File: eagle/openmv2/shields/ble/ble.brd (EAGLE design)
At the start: 35.6 x 26.7 mm, 20 parts, among them U2 OPENMV3

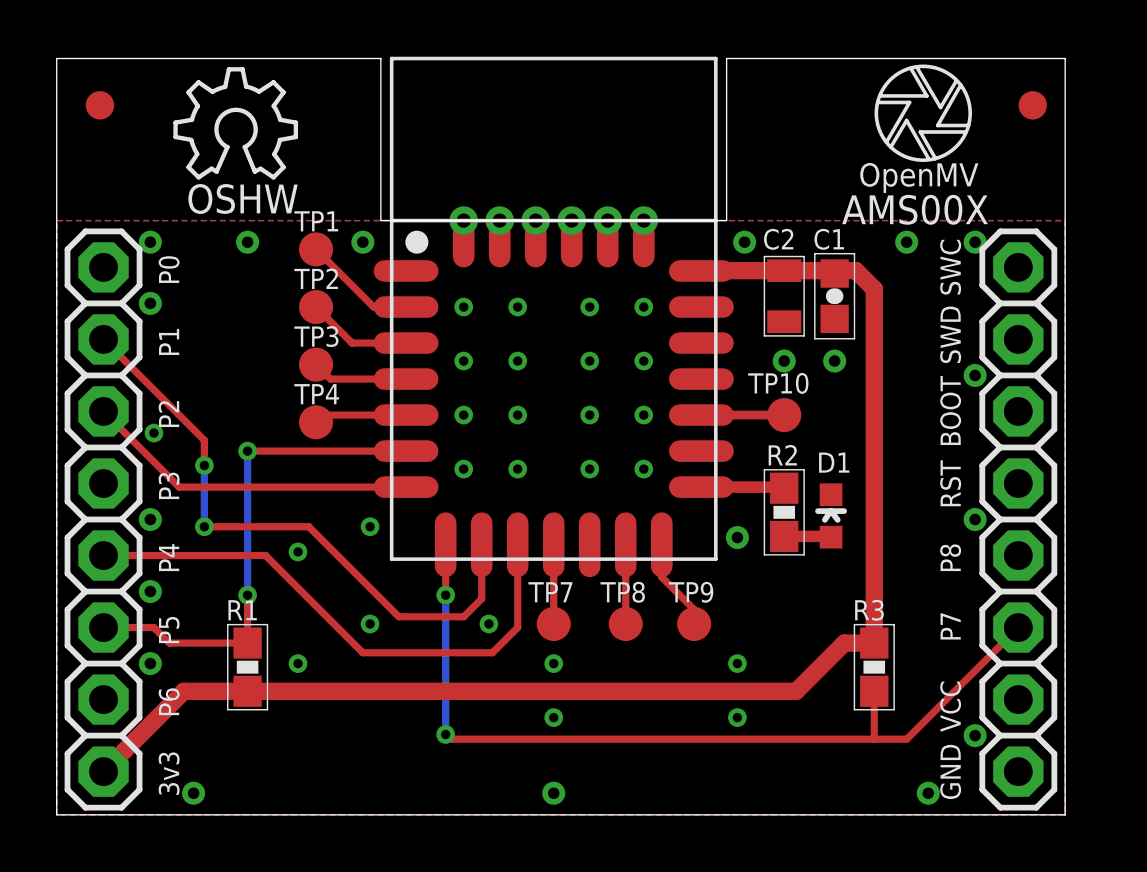
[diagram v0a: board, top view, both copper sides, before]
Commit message: Update shields silk-screen.
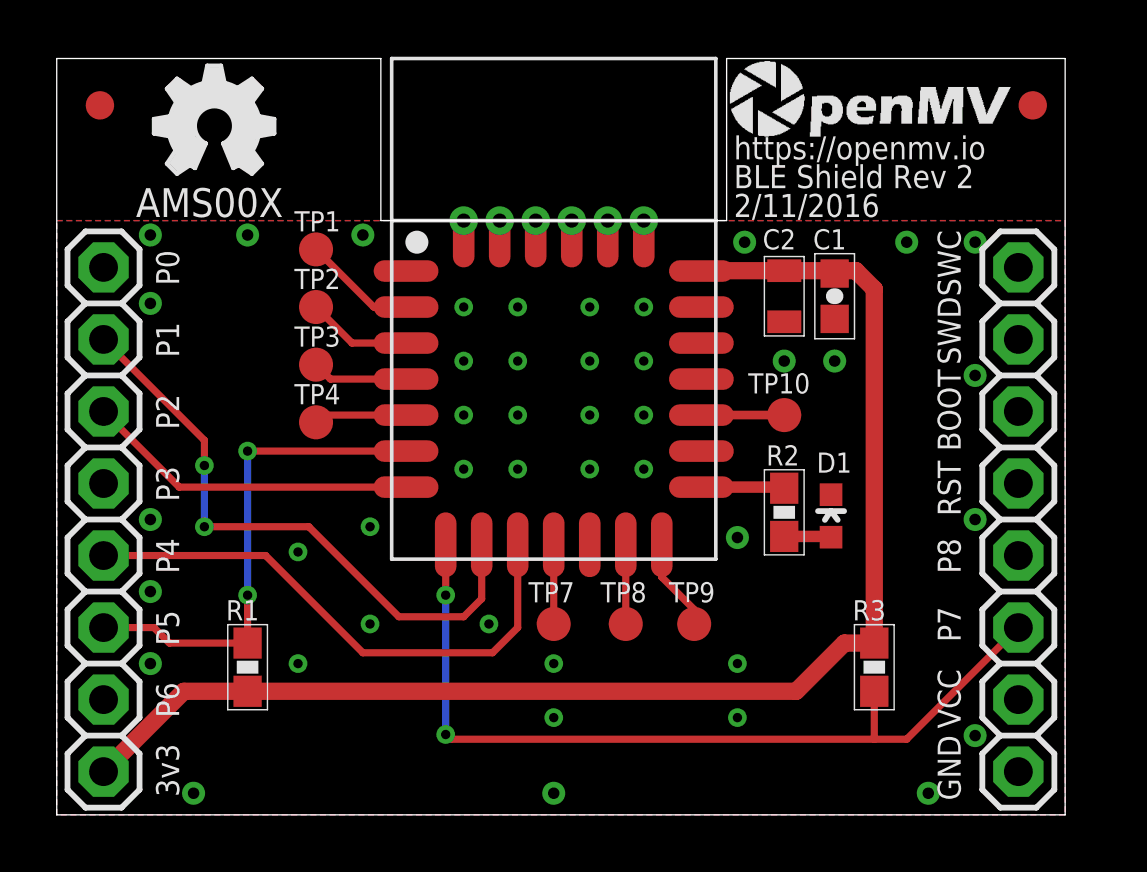
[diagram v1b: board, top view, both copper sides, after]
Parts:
- removed LOGO1: OSHW_LOGO_6MILX0150-NT, iofault:OSHW_6X150_NOTEXT
- added U$5: (no value), iofault:OSHW_FILLX150_NOTEXT
- added U$7: (no value), openmv:OMV-LOGO-SMALL
- added U$8: (no value), openmv:WEEE
- added U$9: (no value), openmv:ROHS
- U$4: value OPENMV-LOGO -> (none); device openmv:OPENMV-LOGO -> openmv:OMV-LOGO
- moved U$4 15.4 mm to (23.7, 8.64), flipped to the bottom
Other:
- board text added: "2/11/2016"
- board text added: "BLE Shield Rev 2"
- board text added: "Built by MacroFab"
- board text added: "Made in USA"
- board text added: "https://openmv.io"
- board text removed: "0.5 oz copper"
- board text removed: "1 oz copper"
- board text removed: "47 mil core"
- board text removed: "6.7 mil prepreg"
- board text removed: "Antenna trace 12mils (50Ohms impedance)"
- board text removed: "OSHW"
- board text removed: "OpenMV"
- board text removed: "Stackup:"
- board text removed: "er is 3.66"
